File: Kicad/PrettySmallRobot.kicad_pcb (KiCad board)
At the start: 2 copper layers, 23 x 28 mm, 52 parts, among them J1 TYPE-C-31-M-12, J2 S2B-PH-K-S(LF)(SN), J3 S2B-PH-K-S(LF)(SN), J4 S2B-PH-K-S(LF)(SN), SW1 SW_Push, SW2 SW_Push, U1 DRV8837, U2 DRV8837, U3 MCP73831-2ACI_MC, U4 ESP32-S2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

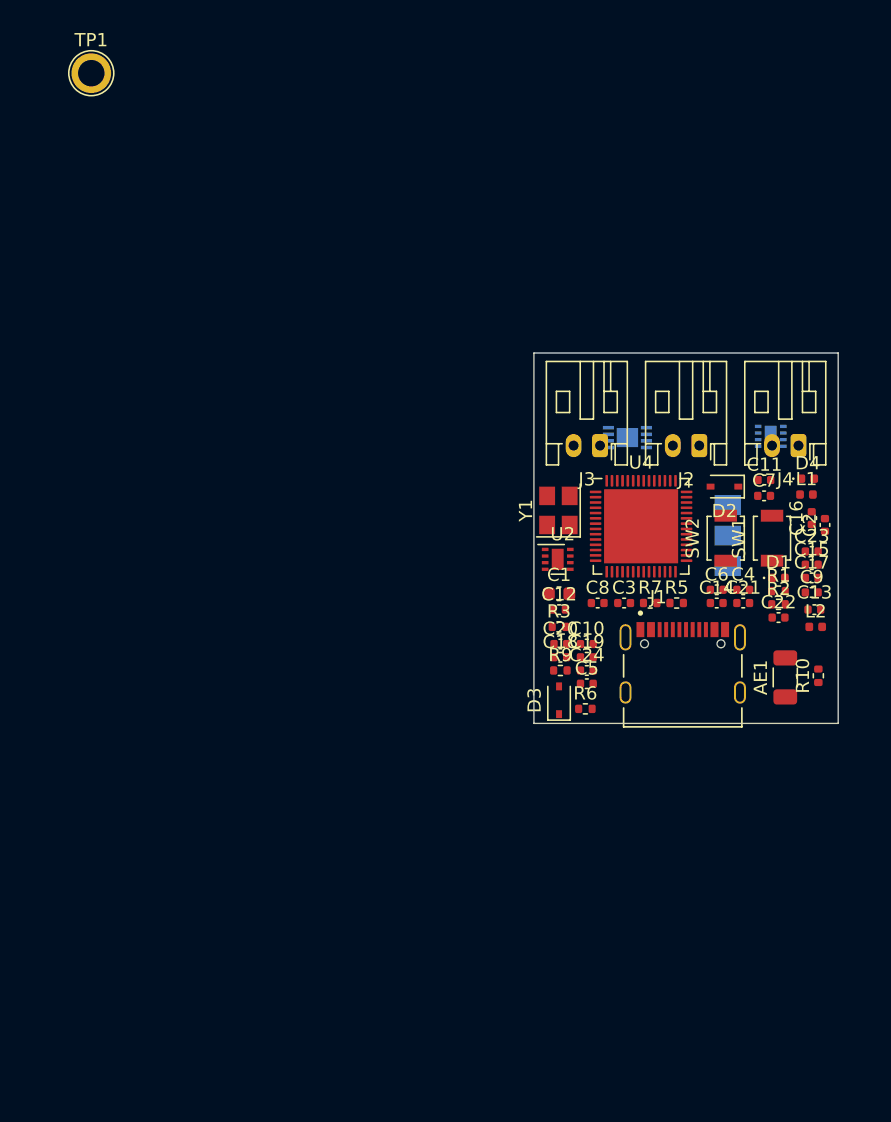
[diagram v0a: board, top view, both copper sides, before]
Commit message: replaced 3.3v ldo with ap2112k
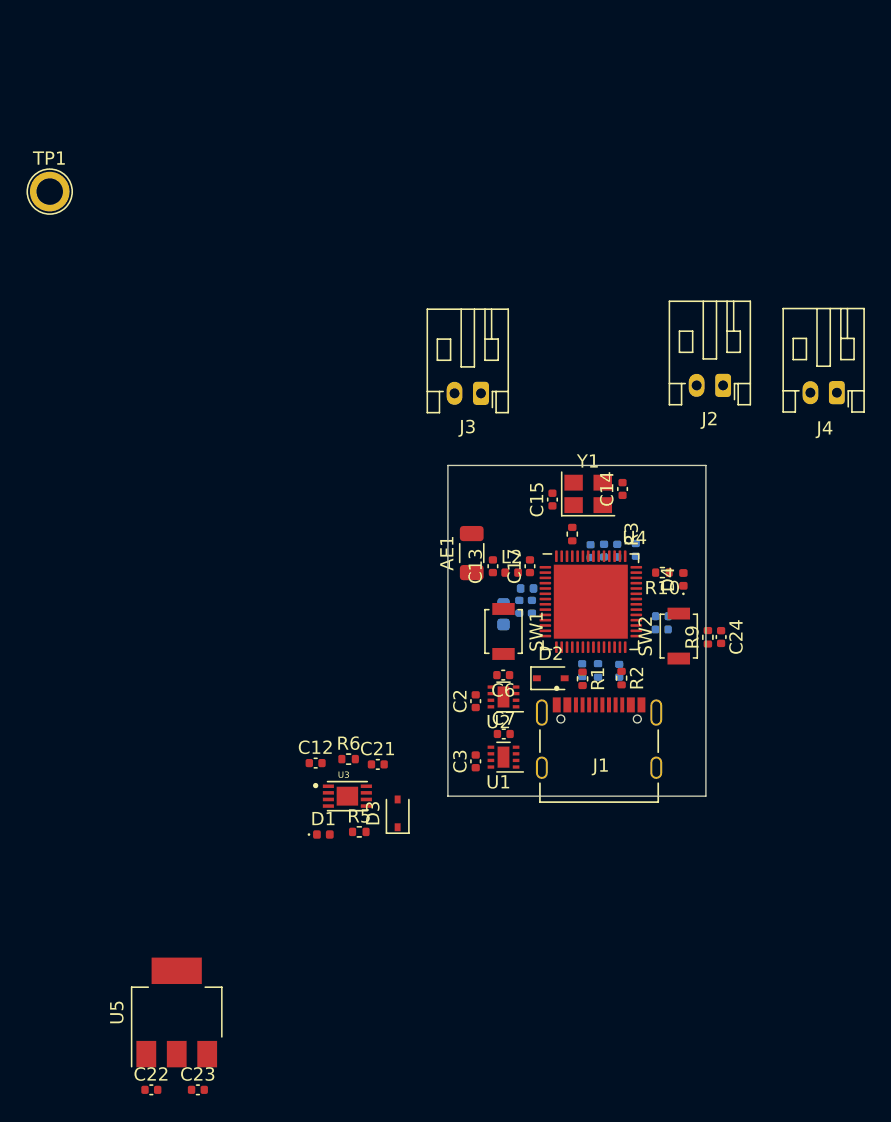
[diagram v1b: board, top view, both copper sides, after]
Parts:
- C1, C10, C11, C16, C18, C19, C20, C4, C5, C8, C9, L1, R7: moved to B.Cu
- U1, U3, U5: moved to F.Cu
- Y1: value 12pf/40MHz -> Crystal_GND24
- moved C23 61.7 mm to (108.6, 143.7)
- moved C22 59.3 mm to (105.1, 143.7)
- moved U5 52.7 mm to (107.0, 137.8), turned to 90 degrees
- moved D1 39.5 mm to (118.1, 124.4)
- moved U3 34.4 mm to (119.9, 121.5), turned to 0 degrees
- moved U1 31.6 mm to (131.7, 118.5), turned to 180 degrees
- moved C21 30.2 mm to (122.2, 119.1)
- moved R5 29.6 mm to (120.8, 124.2)
- moved C2 29.6 mm to (129.6, 114.3)
- moved C7 26.7 mm to (131.7, 116.8)
- moved AE1 25.5 mm to (129.3, 103.1)
- moved C13 24.5 mm to (130.9, 104.1), turned to 90 degrees
- moved L2 23.3 mm to (132.3, 104.6)
- moved L1 22.3 mm to (133.5, 105.8)
- moved C12 21.8 mm to (117.5, 119.0)
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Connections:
- C14 pad 2: Net-(C14-Pad2) -> Net-(U4-Pad52)
- U4 pad 52: Net-(C14-Pad2) -> Net-(U4-Pad52)
- Y1 pad 2: Net-(C14-Pad2) -> GND
- Y1 pad 3: (no net) -> Net-(U4-Pad52)
- Y1 pad 4: (no net) -> GND
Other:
- board size 23 x 28 mm -> 19.5 x 25 mm

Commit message: replaced jst connectors with smd solder pads
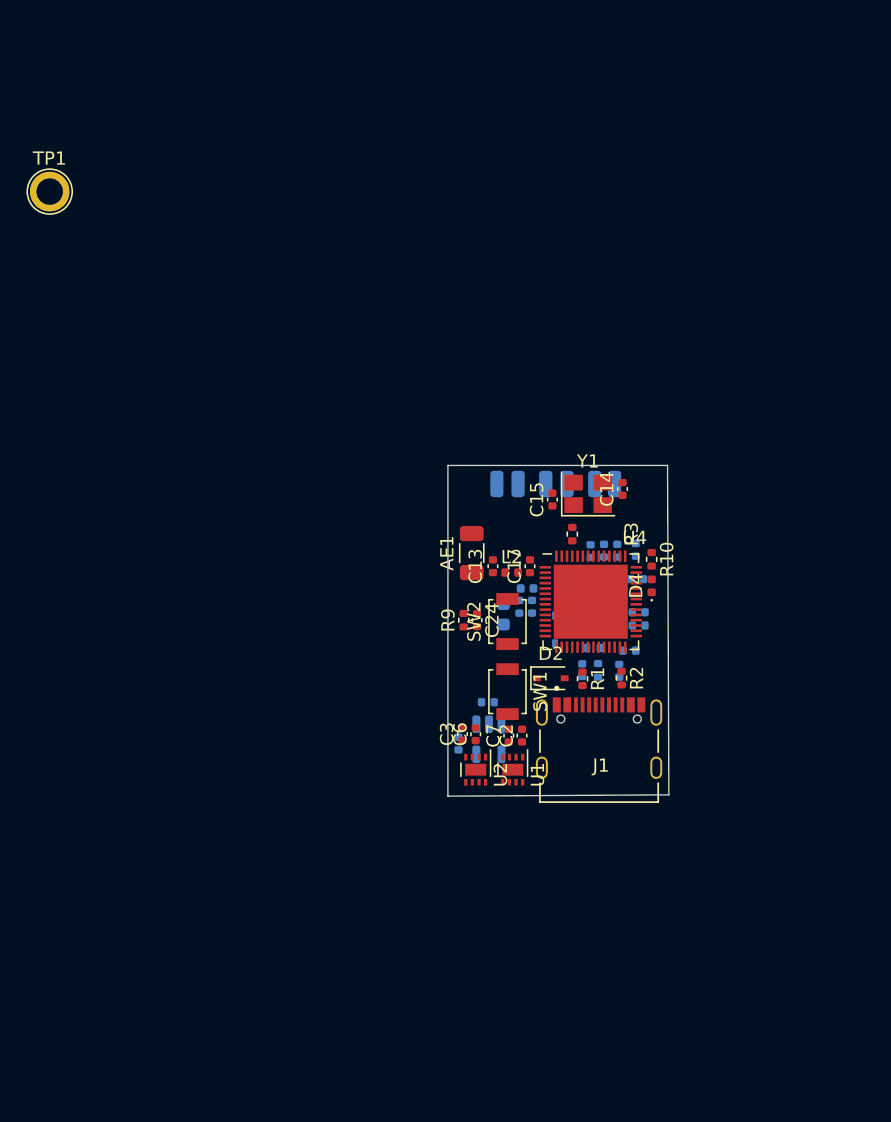
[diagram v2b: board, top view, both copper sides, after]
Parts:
- removed U5: AP2111H-3.3TRG1, Package_TO_SOT_SMD:SOT-223
- added J5: MOTORB_2, Connector_Wire:SolderWirePad_1x01_SMD_1x2mm, B.Cu at (131.2, 97.9)
- added J6: BATT+, Connector_Wire:SolderWirePad_1x01_SMD_1x2mm, B.Cu at (138.6, 97.9)
- added J7: GND, Connector_Wire:SolderWirePad_1x01_SMD_1x2mm, B.Cu at (140.1, 97.9)
- added U6: AP2112K-3.3, Package_TO_SOT_SMD:SOT-23-5, B.Cu at (130.6, 117.2)
- C12, C21, C22, C23, D1, D3, R5, R6, U3: moved to B.Cu
- J2: value S2B-PH-K-S(LF)(SN) -> MOTORA_1; footprint Connector_JST:JST_PH_S2B-PH-K_1x02_P2.00mm_Horizontal -> Connector_Wire:SolderWirePad_1x01_SMD_1x2mm; moved to B.Cu
- J3: value S2B-PH-K-S(LF)(SN) -> MOTORA_2; footprint Connector_JST:JST_PH_S2B-PH-K_1x02_P2.00mm_Horizontal -> Connector_Wire:SolderWirePad_1x01_SMD_1x2mm; moved to B.Cu
- J4: value S2B-PH-K-S(LF)(SN) -> MOTORB_1; footprint Connector_JST:JST_PH_S2B-PH-K_1x02_P2.00mm_Horizontal -> Connector_Wire:SolderWirePad_1x01_SMD_1x2mm; moved to B.Cu
- Y1: value Crystal_GND24 -> 12pF/40MHz
- moved C22 38.8 mm to (130.5, 114.4), turned to 180 degrees
- moved C23 32.8 mm to (128.3, 117.5), turned to 90 degrees
- moved C12 28.0 mm to (141.8, 105.1), turned to 180 degrees
- moved D1 27.0 mm to (141.2, 110.5), turned to 180 degrees
- moved R6 23.8 mm to (139.3, 104.8), turned to 180 degrees
- moved U3 23.5 mm to (138.8, 107.6), turned to 180 degrees
- moved J4 23.1 mm to (134.9, 97.9), turned to 0 degrees
- moved R5 22.5 mm to (138.5, 110.3), turned to 180 degrees
- moved C21 20.4 mm to (137.1, 105.2), turned to 180 degrees
- moved R9 18.5 mm to (128.7, 108.2)
- moved C24 18.5 mm to (129.7, 108.2)
- moved D3 18.3 mm to (135.6, 108.9)
- moved J2 17.2 mm to (132.8, 97.9), turned to 0 degrees
- moved SW2 13.0 mm to (132.0, 108.3)
- moved J3 9.44 mm to (136.5, 97.9), turned to 0 degrees
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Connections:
- J3 pad 1: /MOTORB_OUT1 -> /MOTORA_OUT2
- J4 pad 1: +BATT -> /MOTORB_OUT1
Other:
- board size 19.5 x 25 mm -> 16.7 x 25 mm

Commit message: routing bout 70% done
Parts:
- removed TP1: TEST, TestPoint:TestPoint_Plated_Hole_D2.0mm
- added REF**: MountingHole_3.2mm_M3, MountingHole:MountingHole_3.2mm_M3, F.Cu at (146.0, 98.7)
- added REF**: MountingHole_3.2mm_M3_ISO14580, MountingHole:MountingHole_3.2mm_M3_ISO14580, F.Cu at (125.3, 119.2)
- D1: moved to F.Cu
- moved U2 21.3 mm to (132.7, 98.4), turned to 90 degrees
- moved U1 21.3 mm to (129.8, 98.4)
- moved C21 4.50 mm to (138.7, 109.4)
- moved J6 2.90 mm to (141.5, 97.9)
- moved J7 2.90 mm to (143.0, 97.9)
- moved J2 2.80 mm to (130.0, 97.9)
- moved J5 2.80 mm to (128.4, 97.9)
- moved J3 2.40 mm to (134.1, 97.9)
- moved J4 2.40 mm to (132.5, 97.9)
- moved C19 2.13 mm to (140.3, 103.6), turned to 90 degrees
- moved C20 2.11 mm to (138.3, 103.6), turned to 90 degrees
- moved D1 1.79 mm to (143.0, 110.6), turned to 90 degrees
- moved R6 1.08 mm to (138.7, 105.7)
- moved C18 0.68 mm to (139.3, 103.6), turned to 90 degrees
- moved C7 0.60 mm to (131.5, 116.9)
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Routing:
- net +BATT: track 0.00 -> 20.2 mm, vias 0 -> 2
- net /VDDA: track 0.00 -> 14.2 mm, vias 0 -> 3
- net /VBUS: track 0.00 -> 13.6 mm, vias 0 -> 2
- net +3V3: track 0.00 -> 12.9 mm, vias 0 -> 4
- net Net-(C22-Pad1): track 0.00 -> 12.2 mm, vias 0 -> 1
- net /~{RESET}: track 0.00 -> 11.7 mm, vias 0 -> 2
- net /BOOT: track 0.00 -> 10.6 mm
- net Net-(U4-Pad52): track 0.00 -> 7.85 mm
- net /D-: track 0.00 -> 7.72 mm
- net /D+: track 0.00 -> 6.42 mm
- net Net-(D1-Pad1): track 0.00 -> 4.03 mm, vias 0 -> 1
- net Net-(R3-Pad1): track 0.00 -> 3.26 mm
- net Net-(D4-Pad2): track 0.00 -> 3.22 mm
- net Net-(R5-Pad2): track 0.00 -> 2.77 mm
- net Net-(AE1-Pad1): track 0.00 -> 2.55 mm
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- added copper zone on In2.Cu, net +3V3
- added copper zone on B.Cu, net GND
- added copper zone on F.Cu, net GND
- added copper zone on In1.Cu, net GND
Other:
- board size 16.7 x 25 mm -> 25.6 x 25 mm
- copper layers 2 -> 4

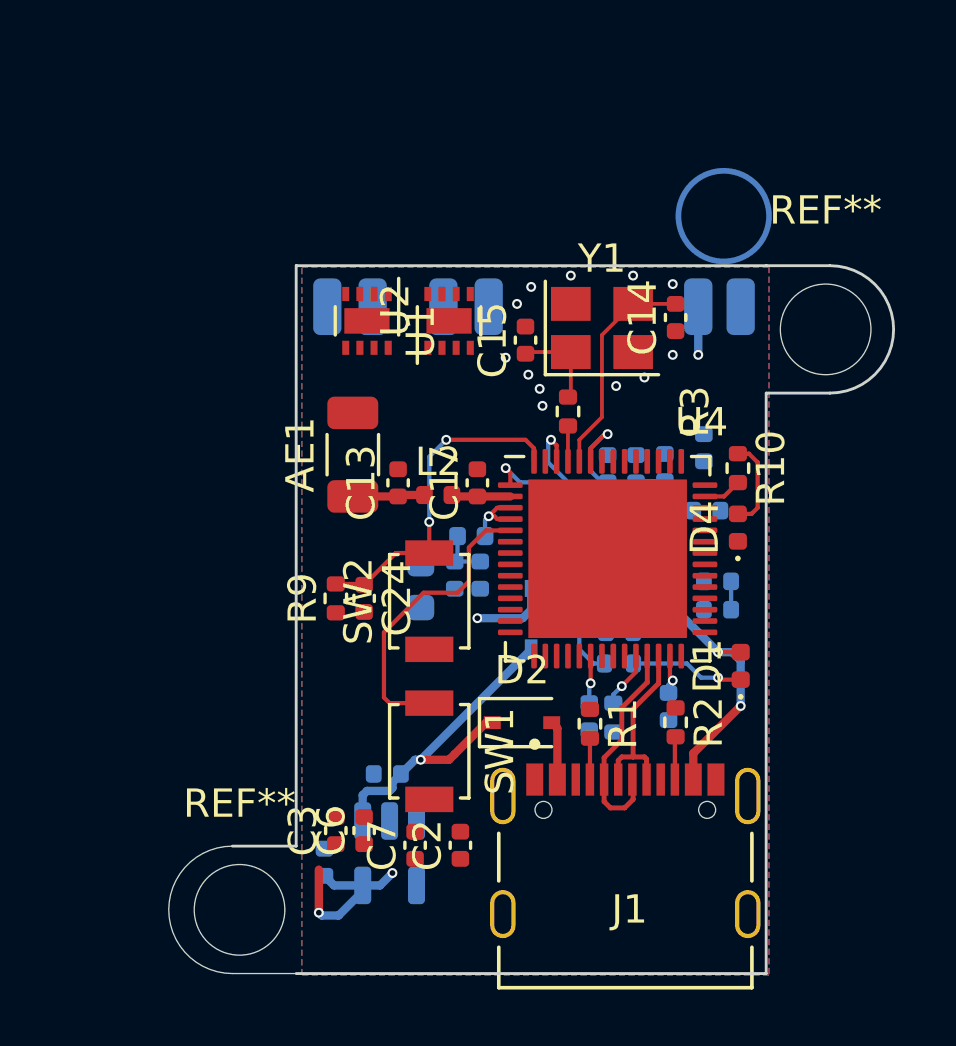
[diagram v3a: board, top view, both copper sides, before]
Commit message: routed motor driver sigs
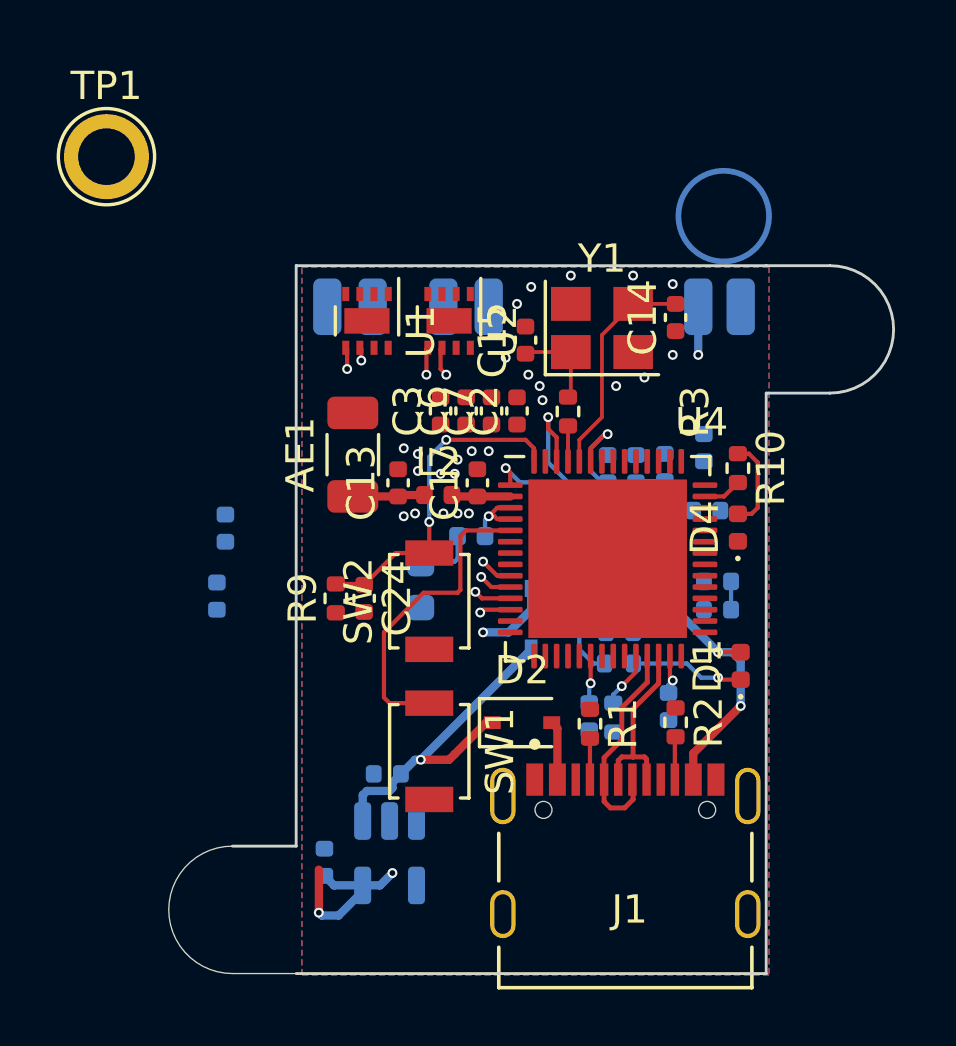
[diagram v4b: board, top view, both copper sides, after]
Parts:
- removed REF**: MountingHole_3.2mm_M3, MountingHole:MountingHole_3.2mm_M3
- removed REF**: MountingHole_3.2mm_M3_ISO14580, MountingHole:MountingHole_3.2mm_M3_ISO14580
- added TP1: TEST, TestPoint:TestPoint_Plated_Hole_D2.0mm, F.Cu at (120.6, 92.6)
- moved C7 15.6 mm to (134.2, 101.6)
- moved C2 15.5 mm to (135.1, 101.6)
- moved C3 15.3 mm to (132.4, 101.6)
- moved C6 15.3 mm to (133.3, 101.6)
- moved C4 9.33 mm to (124.5, 108.1)
- moved C5 8.27 mm to (124.8, 105.7)
- turned U2 to -90 degrees
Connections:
- C2 pad 1: +3V3 -> unconnected-(C2-Pad1)
- C7 pad 1: +3V3 -> +BATT
- U1 pad 5: /MOTORA_IN1 -> /MOTORA_IN2
- U1 pad 7: /DRIVERA_SLEEP -> +3V3
- U2 pad 5: /MOTORB_IN1 -> /MOTORB_IN2
- U2 pad 7: /DRIVERB_SLEEP -> +3V3
- U4 pad 13: /DRIVERA_SLEEP -> unconnected-(U4-Pad13)
- U4 pad 14: /DRIVERB_SLEEP -> unconnected-(U4-Pad14)
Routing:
- net /MOTORA_IN2: track 0.00 -> 15.6 mm, vias 0 -> 2
- net /MOTORB_IN2: track 0.00 -> 15.0 mm, vias 0 -> 2
- net /MOTORA_IN1: track 0.00 -> 14.2 mm, vias 0 -> 2
- net /MOTORB_IN1: track 0.00 -> 13.2 mm, vias 0 -> 2
- net /VDDA: track 14.2 -> 15.8 mm
- net +3V3: track 12.9 -> 12.0 mm
- net GND: vias 12 -> 25

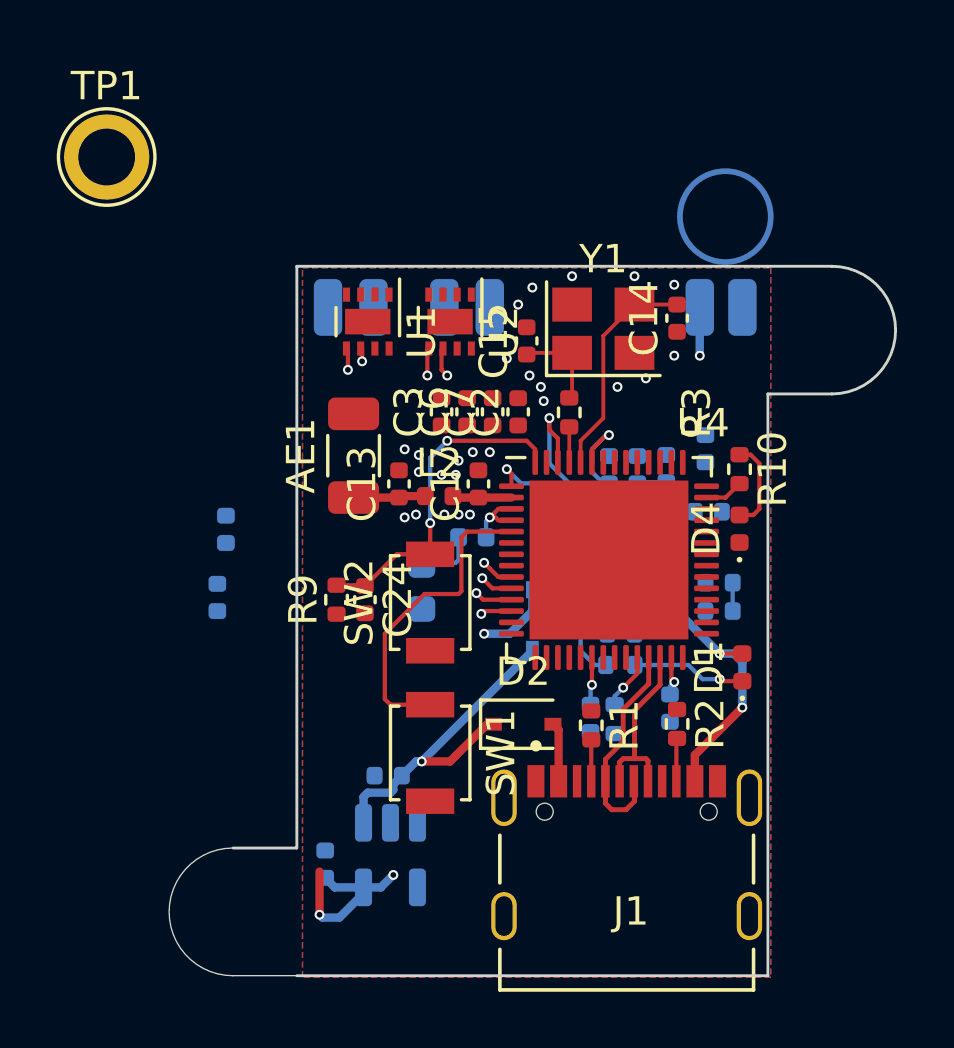
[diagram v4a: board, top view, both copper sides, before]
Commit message: fixed drc issues
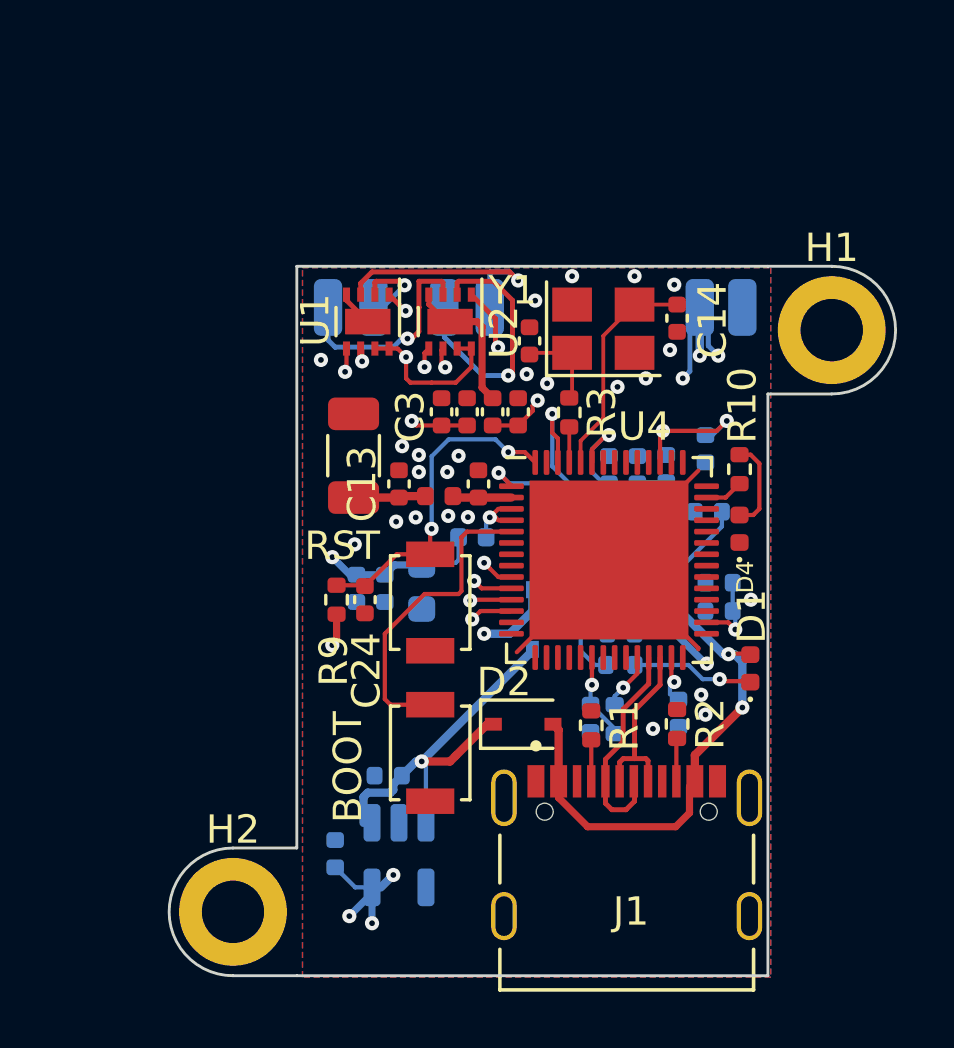
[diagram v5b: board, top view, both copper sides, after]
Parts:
- removed TP1: TEST, TestPoint:TestPoint_Plated_Hole_D2.0mm
- added H1: MountingHole, MountingHole:MountingHole_2.2mm_M2_DIN965_Pad, F.Cu at (146.2, 98.7)
- added H2: MountingHole, MountingHole:MountingHole_2.2mm_M2_DIN965_Pad, F.Cu at (125.0, 119.2)
- moved C4 5.91 mm to (130.4, 107.8)
- moved C5 5.05 mm to (129.4, 107.8)
- moved C23 0.51 mm to (128.7, 117.2)
- moved R6 0.46 mm to (138.8, 105.2)
- moved C9 0.35 mm to (140.8, 112.2)
- moved U6 0.30 mm to (130.9, 117.2)
- moved D1 0.28 mm to (143.3, 110.6)
- moved C15 0.10 mm to (135.5, 99.1)
- renumbered SW1 to BOOT, SW2 to RST
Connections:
- C2 pad 1: unconnected-(C2-Pad1) -> +BATT
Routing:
- net +BATT: track 20.2 -> 64.8 mm, vias 2 -> 8
- net +3V3: track 12.0 -> 35.6 mm, vias 4 -> 11
- net GND: track 0.00 -> 22.1 mm, vias 25 -> 24
- net /VBUS: track 13.6 -> 22.9 mm
- net /MOTORB_OUT1: track 0.00 -> 9.24 mm, vias 0 -> 1
- net /MOTORA_OUT2: track 0.00 -> 8.61 mm, vias 0 -> 1
- net /MOTORB_OUT2: track 0.00 -> 7.75 mm, vias 0 -> 1
- net /MOTORA_OUT1: track 0.00 -> 2.98 mm, vias 0 -> 1
- net Net-(C22-Pad1): track 12.2 -> 14.5 mm
- net /VDD_SPI: track 1.00 -> 2.80 mm, vias 0 -> 1
- net /MOTORB_IN2: track 15.0 -> 16.0 mm
